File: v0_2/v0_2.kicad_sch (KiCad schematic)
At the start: 12 parts, among them IC1 RASPBERRY_PI_PICO_W

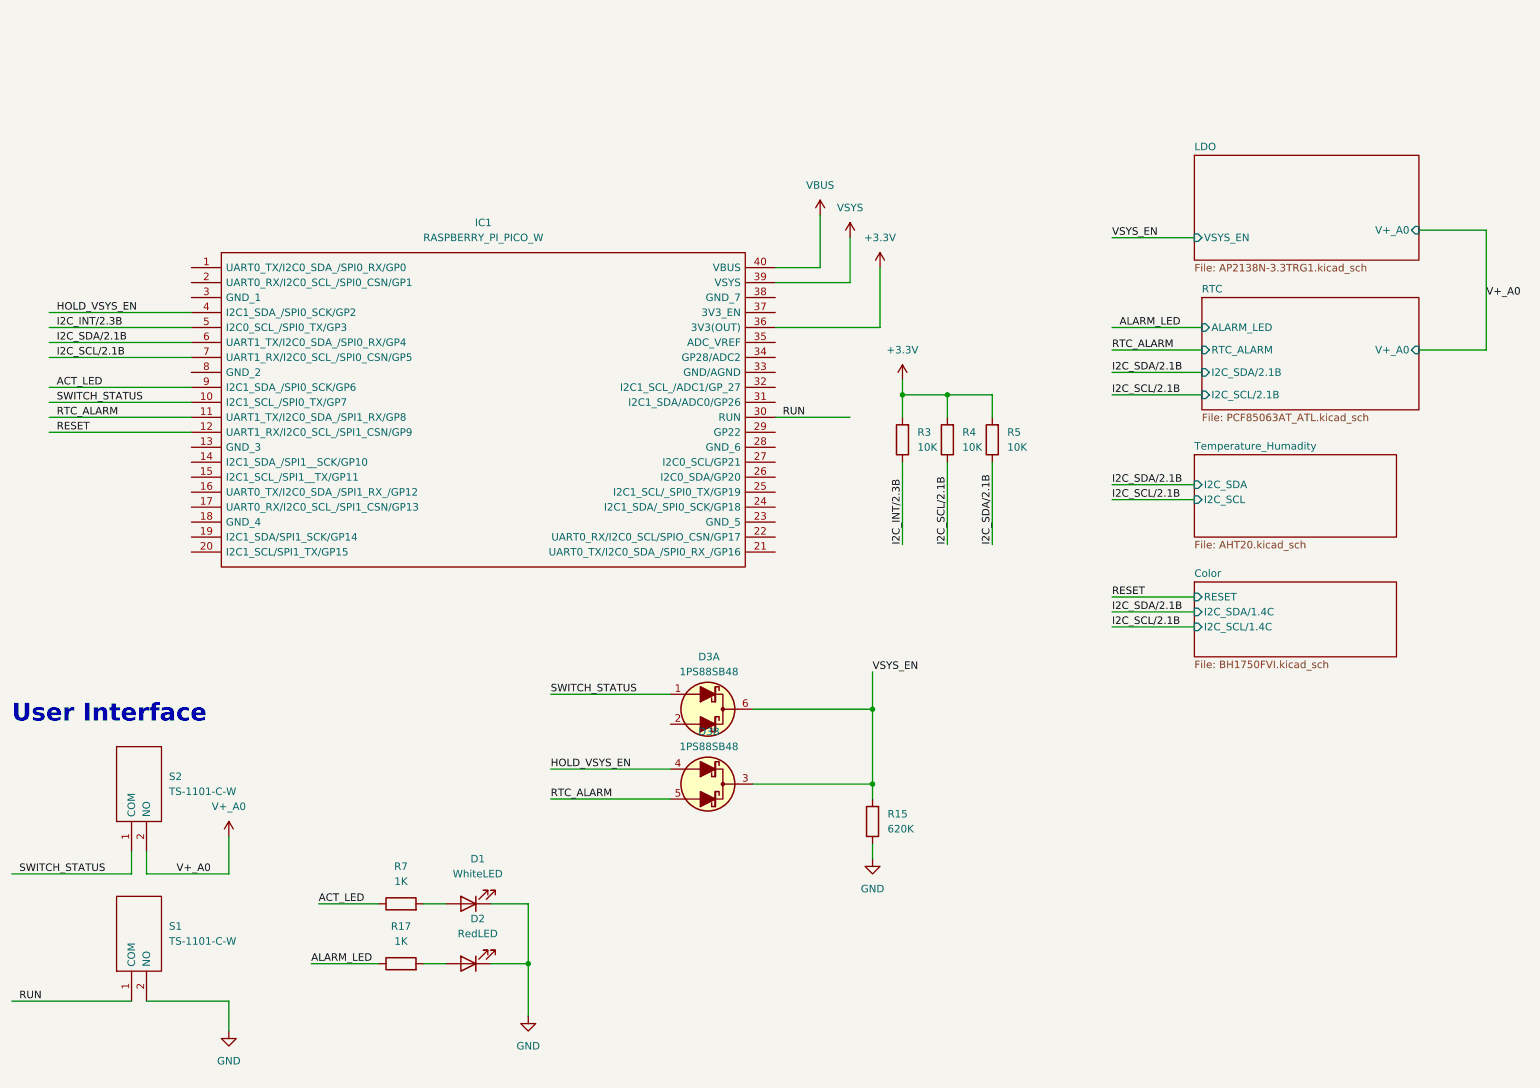
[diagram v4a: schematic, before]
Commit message: add sdcard socket
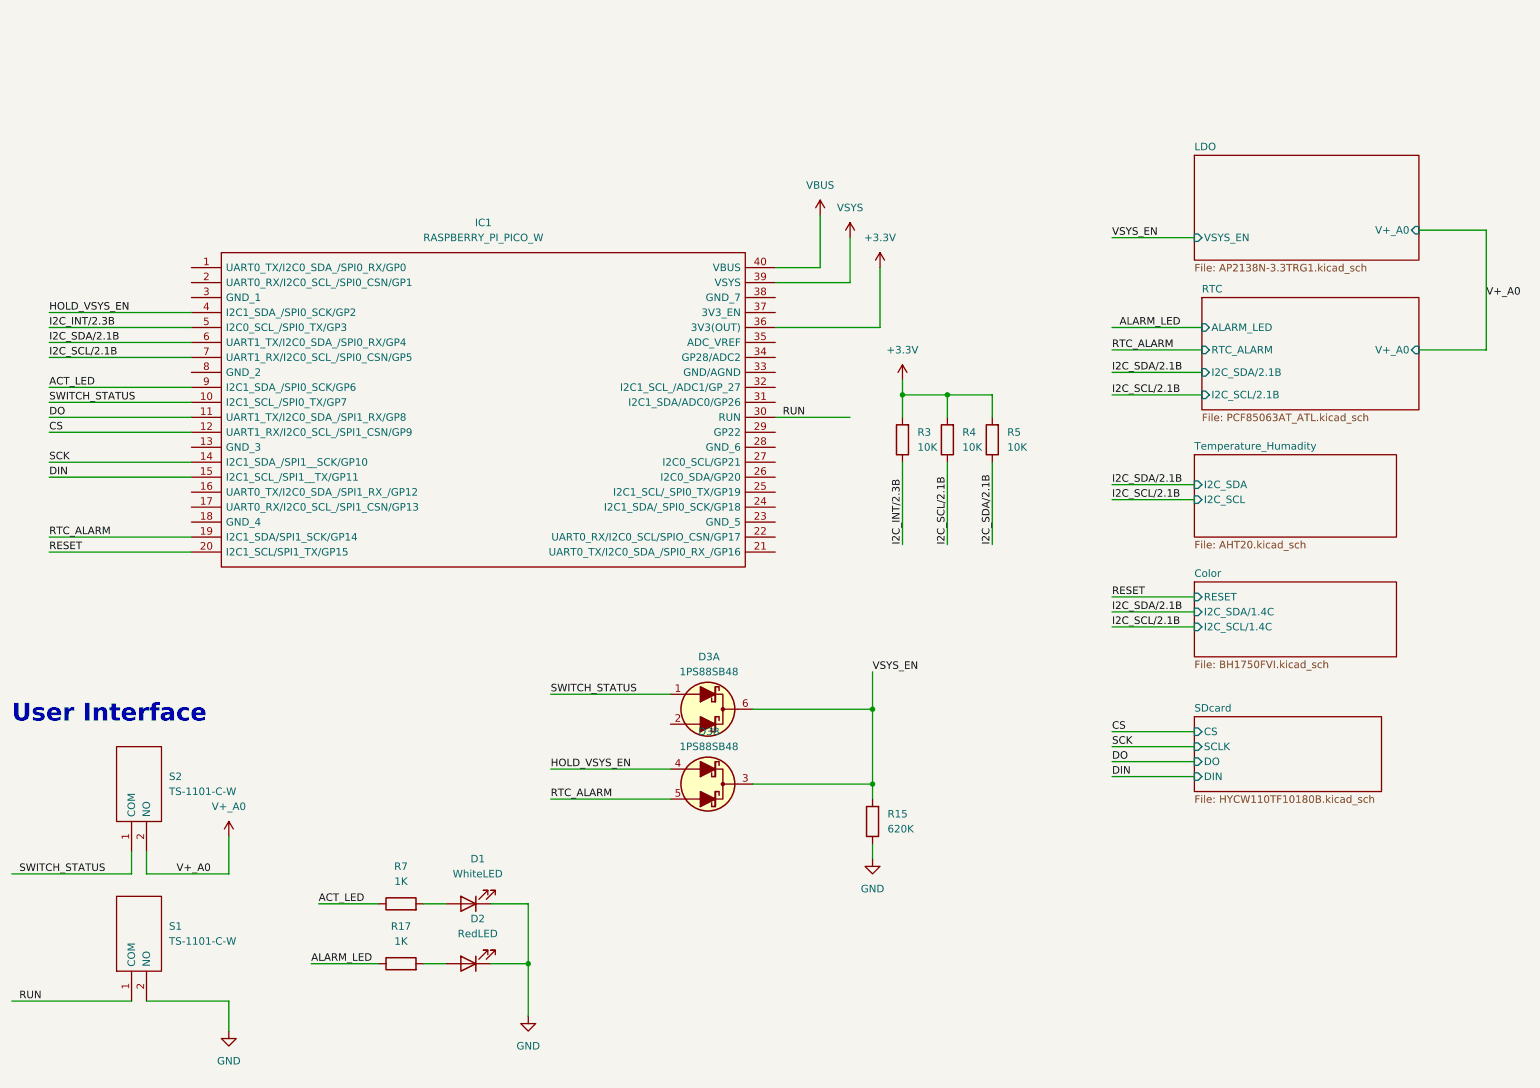
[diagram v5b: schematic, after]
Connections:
- net RESET: now also IC1.20 (I2C1_SCL/SPI1_TX/GP15); no longer IC1.12 (UART1_RX/I2C0_SCL_/SPI1_CSN/GP9)
- net RTC_ALARM: now also IC1.19 (I2C1_SDA/SPI1_SCK/GP14); no longer IC1.11 (UART1_TX/I2C0_SDA_/SPI1_RX/GP8)
- net SCK: now reaches IC1.14 (I2C1_SDA_/SPI1__SCK/GP10)
- net DIN: now reaches IC1.15 (I2C1_SCL_/SPI1__TX/GP11)
- new net CS: IC1.12 (UART1_RX/I2C0_SCL_/SPI1_CSN/GP9)
- new net DO: IC1.11 (UART1_TX/I2C0_SDA_/SPI1_RX/GP8)
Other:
- added sheet SDcard (HYCW110TF10180B.kicad_sch)

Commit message: for quoate
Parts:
- added H1, H2, H3, H4: MountingHole_Pad, MountingHole:MountingHole_2.2mm_M2_Pad_TopBottom, symbol Mechanical:MountingHole_Pad
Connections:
- net GND: now also H1.1, H2.1, H3.1, H4.1
- net DIN renamed MOSI
- net DO renamed MISO

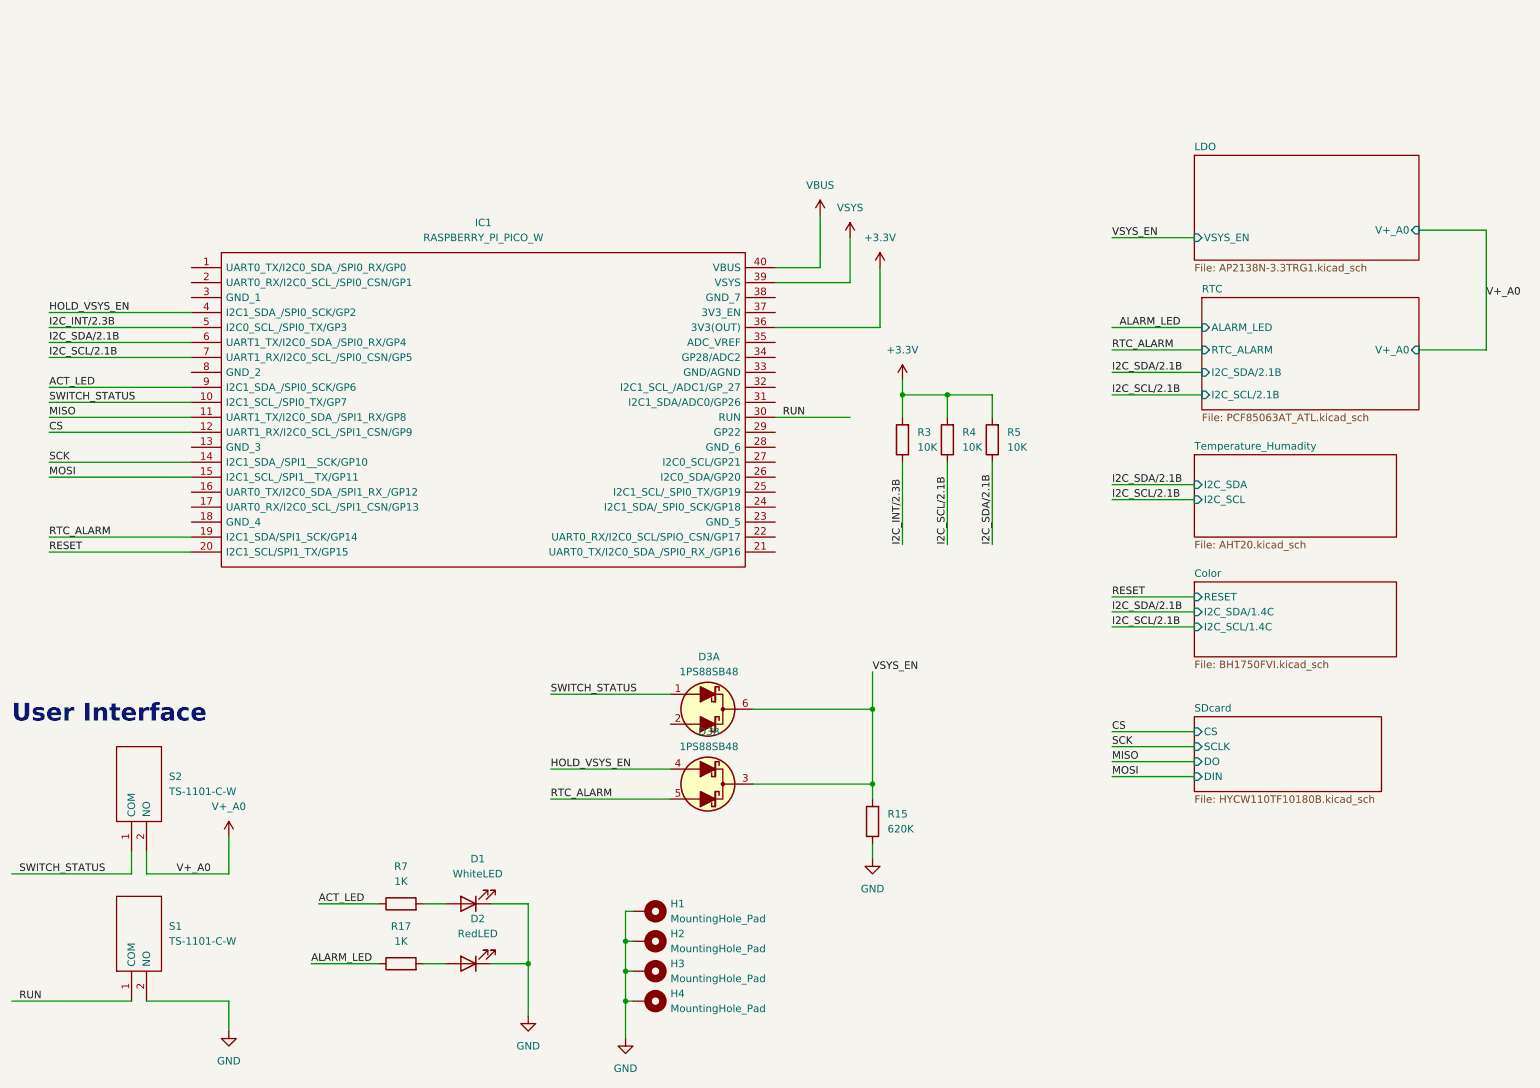
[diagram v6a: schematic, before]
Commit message: rename i2c and add button
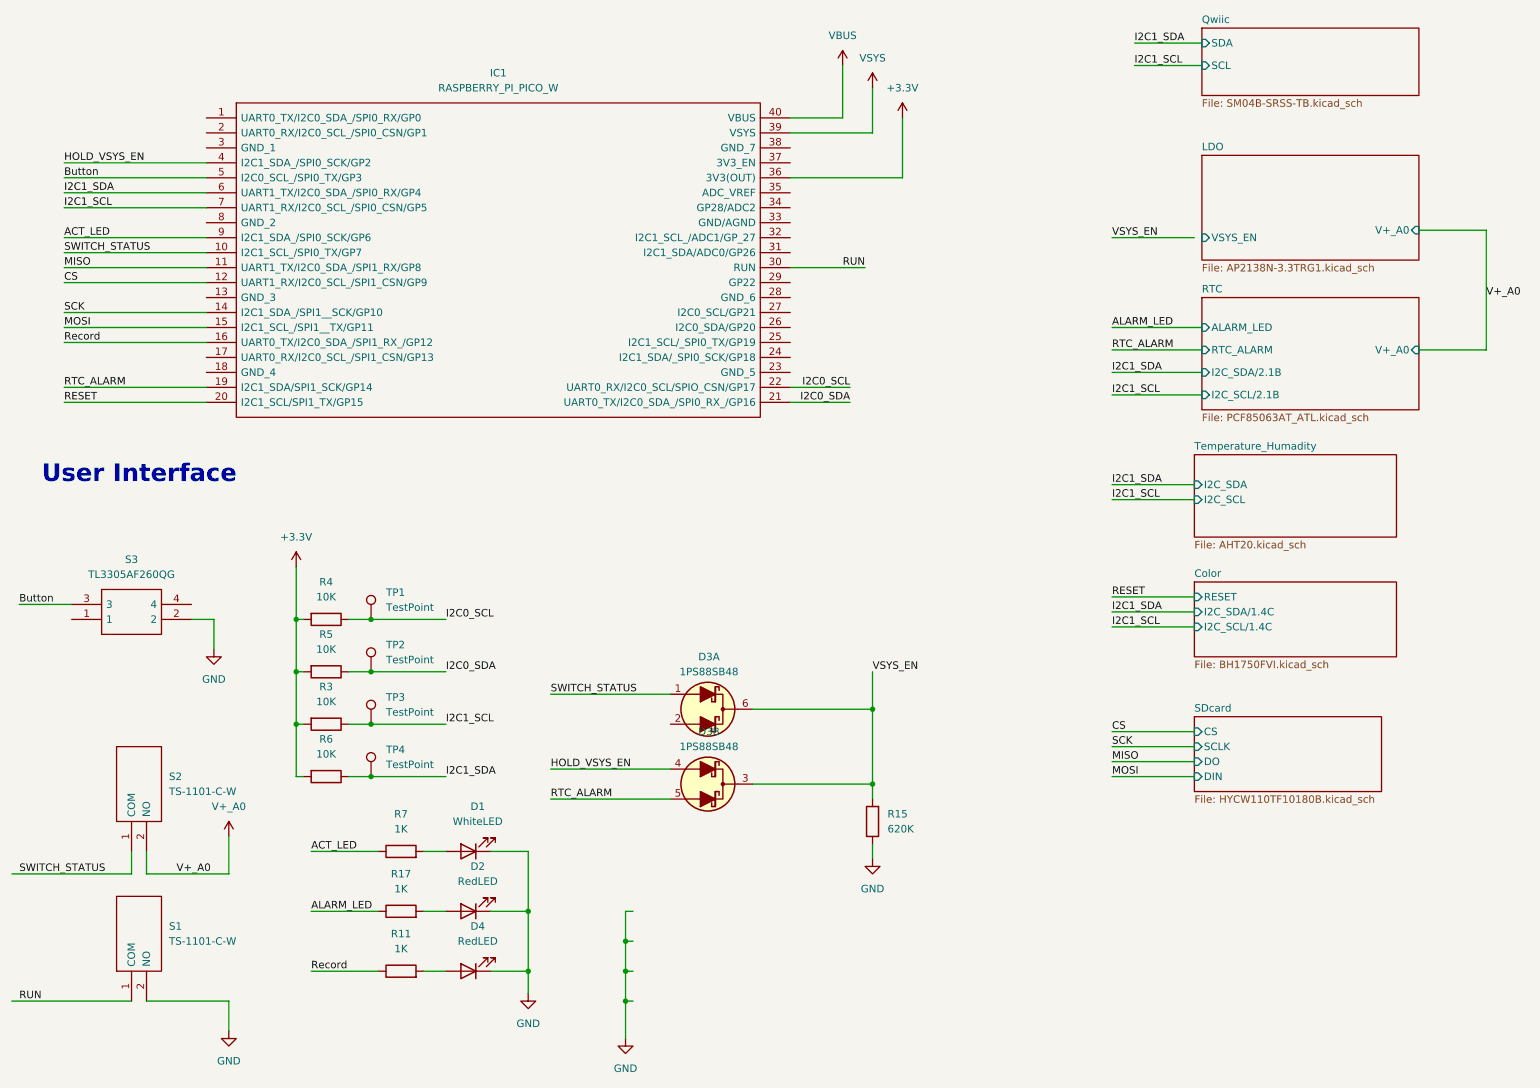
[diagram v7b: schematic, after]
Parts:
- removed H1, H2, H3, H4: MountingHole_Pad, MountingHole:MountingHole_2.2mm_M2_Pad_TopBottom, symbol Mechanical:MountingHole_Pad
- added D4: RedLED, LED_SMD:LED_0603_1608Metric, symbol Device:LED
- added R11: 1K, Resistor_SMD:R_0603_1608Metric, symbol Device:R
- added R6: 10K, Resistor_SMD:R_0603_1608Metric, symbol Device:R
- added S3: TL3305AF260QG, TL3305AF260QG:TL3305AF160QG, symbol TL3305AF260QG:TL3305AF260QG
- added TP1, TP2, TP3, TP4: TestPoint, TestPoint:TestPoint_Pad_D1.0mm, symbol Connector:TestPoint
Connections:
- net +3.3V: now also R6.2
- net GND: now also D4.1 (K), S3.2
- net Record: now reaches IC1.16 (UART0_TX/I2C0_SDA_/SPI1_RX_/GP12)
- net Record: now also R11.1
- net I2C0_SDA: now reaches IC1.21 (UART0_TX/I2C0_SDA_/SPI0_RX_/GP16)
- net I2C0_SDA: now also R5.1, TP2.1
- net I2C0_SCL: now reaches IC1.22 (UART0_RX/I2C0_SCL/SPIO_CSN/GP17)
- net I2C0_SCL: now also R4.1, TP1.1
- net I2C_INT/2.3B renamed Button
- net Button: now also S3.3; no longer R3.1
- net I2C_SCL/2.1B renamed I2C1_SCL
- net I2C1_SCL: now also R3.1, TP3.1; no longer R4.1
- net I2C_SDA/2.1B renamed I2C1_SDA
- net I2C1_SDA: now also R6.1, TP4.1; no longer R5.1
- new net: D4.2 (A), R11.2
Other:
- added sheet Qwiic (SM04B-SRSS-TB.kicad_sch)
- moved on the sheet: D1, D2, IC1, R17, R4, R5, R7

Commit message: add name and button part
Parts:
- added R13: 10K, Resistor_SMD:R_0603_1608Metric, symbol Device:R
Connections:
- net +3.3V: now also S3.4
- net Button: now also S3.1; no longer S3.3
- net GND: now also R13.1; no longer S3.2
- new net: R13.2, S3.2
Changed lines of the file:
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@@
+    (stroke (width 0) (type default))
+  )
+  (wire (pts (xy 57.15 119.38) (xy 58.42 119.38))
     (stroke (width 0) (type default))
   )
@@
     (stroke (width 0) (type default))
   )
+  (wire (pts (xy 48.26 116.84) (xy 58.42 116.84))
+    (stroke (width 0) (type default))
+  )
   (wire (pts (xy 26.67 69.85) (xy 50.8 69.85))
     (stroke (width 0) (type default))
@@
     (stroke (width 0) (type default))
   )
-  (wire (pts (xy 19.05 116.84) (xy 27.94 116.84))
-    (stroke (width 0) (type default))
-  )
   (wire (pts (xy 163.83 147.32) (xy 163.83 134.62))
     (stroke (width 0) (type default))
@@
     (stroke (width 0) (type default))
   )
+  (wire (pts (xy 58.42 116.84) (xy 58.42 111.76))
+    (stroke (width 0) (type default))
+  )
   (wire (pts (xy 168.91 44.45) (xy 168.91 34.29))
     (stroke (width 0) (type default))
@@
     (stroke (width 0) (type default))
   )
-  (wire (pts (xy 48.26 119.38) (xy 52.07 119.38))
+  (wire (pts (xy 48.26 119.38) (xy 49.53 119.38))
     (stroke (width 0) (type default))
   )
@@
     (stroke (width 0) (type default))
   )
+  (wire (pts (xy 19.05 119.38) (xy 27.94 119.38))
+    (stroke (width 0) (type default))
+  )
   (wire (pts (xy 204.47 143.51) (xy 218.44 143.51))
     (stroke (width 0) (type default))
@@
     (stroke (width 0) (type default))
   )
-  (wire (pts (xy 52.07 119.38) (xy 52.07 124.46))
+  (wire (pts (xy 58.42 119.38) (xy 58.42 132.08))
     (stroke (width 0) (type default))
   )
@@
     (effects (font (size 1.27 1.27)) (justify left bottom))
   )
-  (label "Button" (at 19.05 116.84 0) (fields_autoplaced)
-    (effects (font (size 1.27 1.27)) (justify left bottom))
-  )
   (label "ALARM_LED" (at 68.58 168.91 0) (fields_autoplaced)
     (effects (font (size 1.27 1.27)) (justify left bottom))
@@
   )
   (label "SCK" (at 204.47 140.97 0) (fields_autoplaced)
+    (effects (font (size 1.27 1.27)) (justify left bottom))
+  )
+  (label "Button" (at 19.05 119.38 0) (fields_autoplaced)
     (effects (font (size 1.27 1.27)) (justify left bottom))
   )
@@
     )
   )
-  (symbol (lib_id "power:GND") (at 52.07 124.46 0) (unit 1)
-    (in_bom yes) (on_board yes) (dnp no) (fields_autoplaced)
-    (property "Reference" "#PWR032" (at 52.07 130.81 0)
-      (effects (font (size 1.27 1.27)) hide)
-    )
-    (property "Value" "GND" (at 52.07 129.54 0)
-      (effects (font (size 1.27 1.27)))
-    )
-    (property "Footprint" "" (at 52.07 124.46 0)
-      (effects (font (size 1.27 1.27)) hide)
-    )
-    (property "Datasheet" "" (at 52.07 124.46 0)
+  (symbol (lib_id "power:GND") (at 58.42 132.08 0) (unit 1)
+    (in_bom yes) (on_board yes) (dnp no) (fields_autoplaced)
+    (property "Reference" "#PWR032" (at 58.42 138.43 0)
+      (effects (font (size 1.27 1.27)) hide)
+    )
+    (property "Value" "GND" (at 58.42 137.16 0)
+      (effects (font (size 1.27 1.27)))
+    )
+    (property "Footprint" "" (at 58.42 132.08 0)
+      (effects (font (size 1.27 1.27)) hide)
+    )
+    (property "Datasheet" "" (at 58.42 132.08 0)
       (effects (font (size 1.27 1.27)) hide)
     )
@@
     )
   )
+  (symbol (lib_id "Device:R") (at 53.34 119.38 270) (unit 1)
+    (in_bom yes) (on_board yes) (dnp no)
+    (property "Reference" "R13" (at 53.34 121.92 90)
+      (effects (font (size 1.27 1.27)))
+    )
+    (property "Value" "10K" (at 53.34 124.46 90)
+      (effects (font (size 1.27 1.27)))
+    )
+    (property "Footprint" "Resistor_SMD:R_0603_1608Metric" (at 53.34 117.602 90)
+      (effects (font (size 1.27 1.27)) hide)
+    )
+    (property "Datasheet" "~" (at 53.34 119.38 0)
+      (effects (font (size 1.27 1.27)) hide)
+    )
+    (property "Manufacturer_Part_Number" "0603WAF1002T5E" (at 53.34 119.38 90)
+      (effects (font (size 1.27 1.27)) hide)
+    )
+    (pin "1")
+    (pin "2")
+    (instances
+      (project "v0_2"
+        (path "/678523e5-508b-4706-b0e0-f17e466a8d09"
+          (reference "R13") (unit 1)
+        )
+      )
+    )
+  )
   (symbol (lib_id "power:GND") (at 54.61 189.23 0) (unit 1)
     (in_bom yes) (on_board yes) (dnp no) (fields_autoplaced)
@@
         )
       )
+    )
+  )
+  (symbol (lib_id "power:+3.3V") (at 58.42 111.76 0) (unit 1)
+    (in_bom yes) (on_board yes) (dnp no) (fields_autoplaced)
+    (property "Reference" "#PWR033" (at 58.42 115.57 0)
+      (effects (font (size 1.27 1.27)) hide)
+    )
+    (property "Value" "+3.3V" (at 58.42 106.68 0)
+      (effects (font (size 1.27 1.27)))
+    )
+    (property "Footprint" "" (at 58.42 111.76 0)
+      (effects (font (size 1.27 1.27)) hide)
+    )
+    (property "Datasheet" "" (at 58.42 111.76 0)
+      (effects (font (size 1.27 1.27)) hide)
+    )
+    (pin "1")
+    (instances
+      (project "v0_2"
+        (path "/678523e5-508b-4706-b0e0-f17e466a8d09"
+          (reference "#PWR033") (unit 1)
+        )
+      )
